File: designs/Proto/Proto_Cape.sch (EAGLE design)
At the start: 24 parts

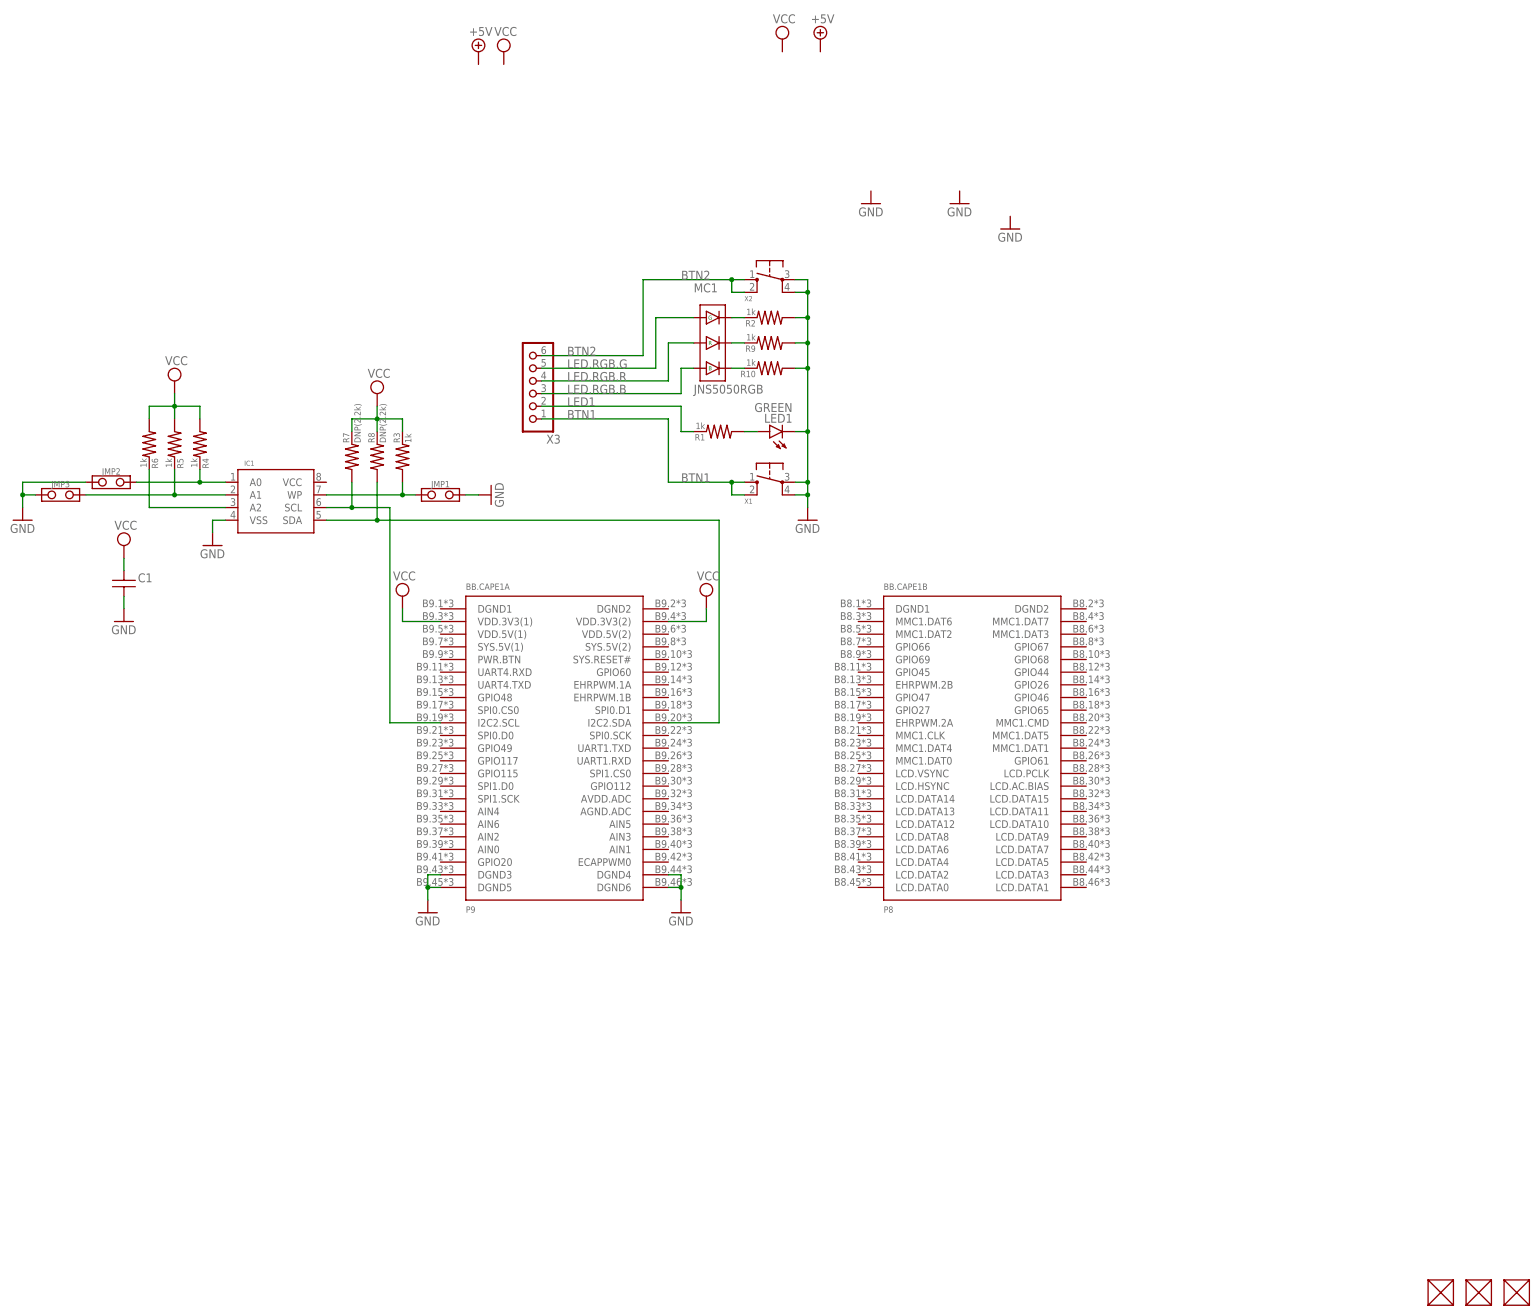
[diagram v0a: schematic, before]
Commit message: Added the revised EAGLE schematics. Also removed two files that were probably not intended to be added as they are lock files in EAGLE.
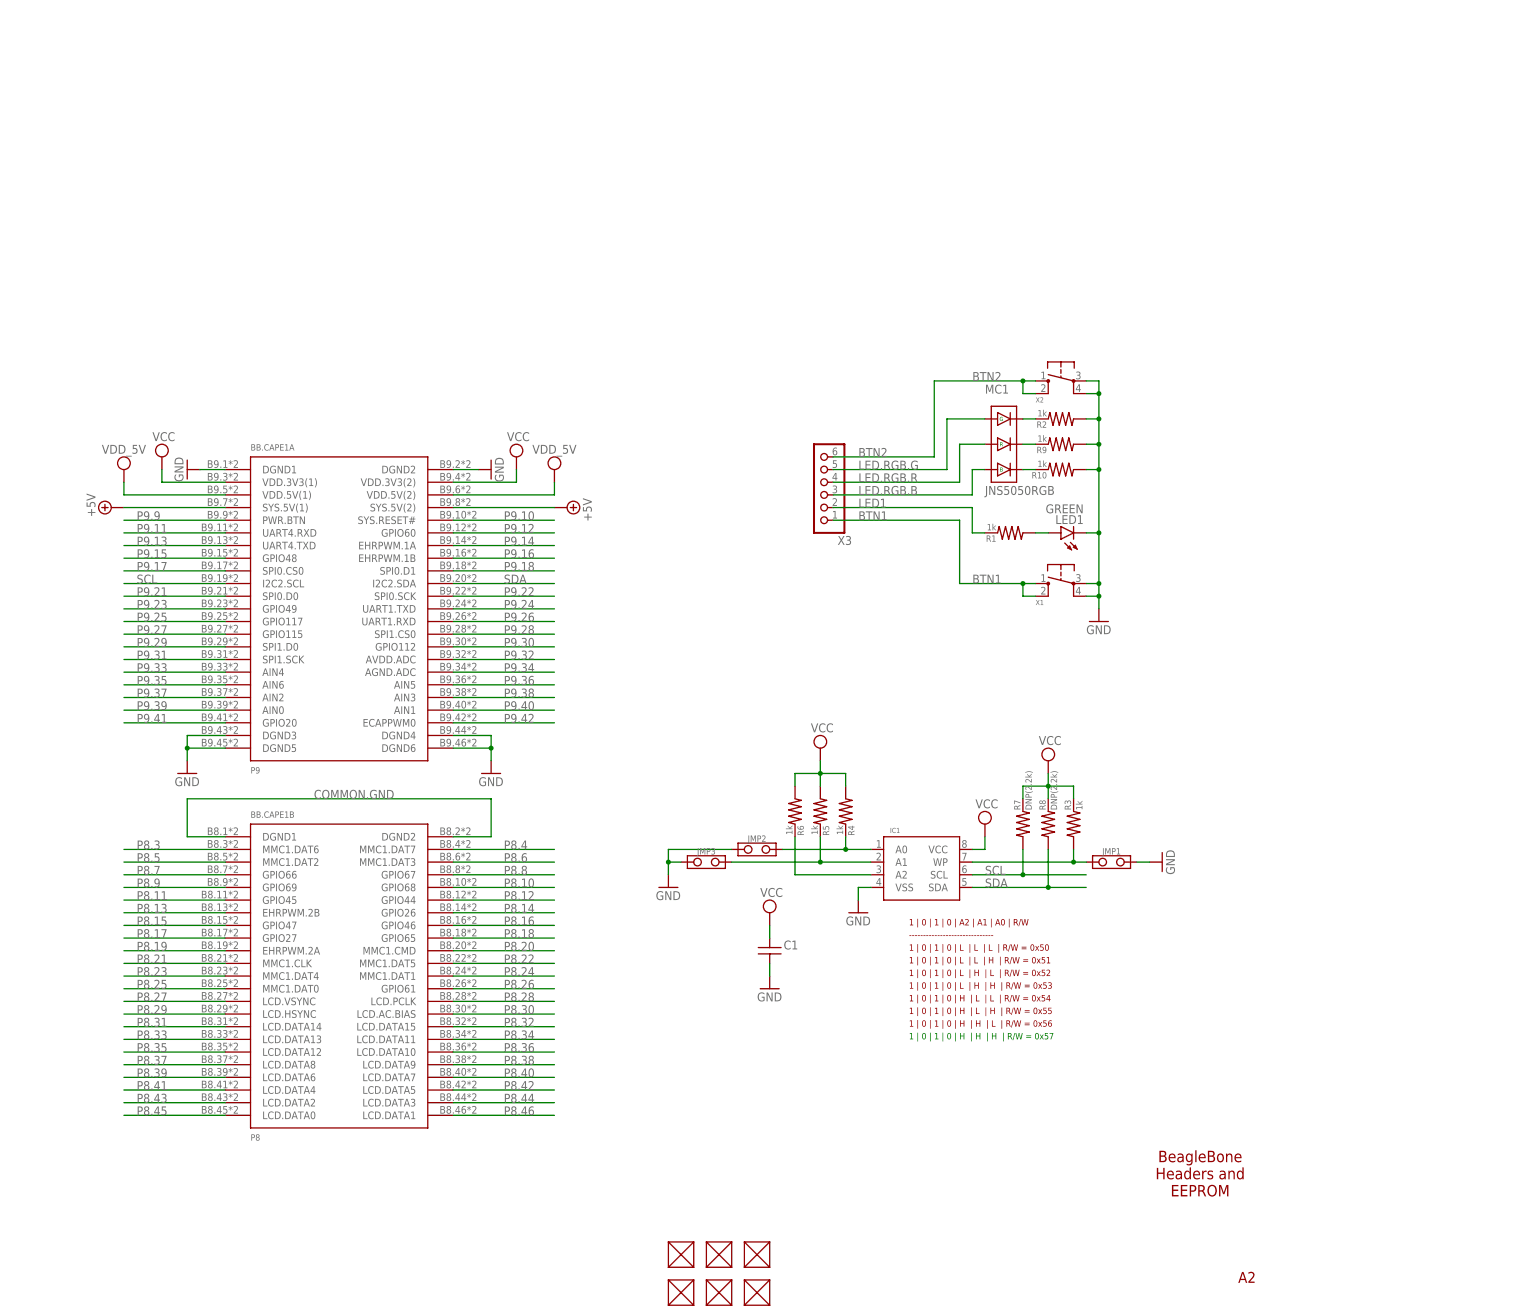
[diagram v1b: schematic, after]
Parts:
- added FUD4, FUD5, FUD6: FIDUCIAL, GHI:FIDUCIAL
- BB.CAPE1: value BEAGLEBONE.CAPE.TOP/BOTTOM-PADS/W/TH -> BEAGLEBONE.CAPE.TOP/BOTTOM-PADS; device GHI-Solutions:BEAGLEBONE.CAPE.TOP/BOTTOM-PADS/W/TH -> GHI-Solutions:BEAGLEBONE.CAPE.TOP/BOTTOM-PADS
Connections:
- new net +5V: BB.CAPE1A.SYS.5V(1), BB.CAPE1A.SYS.5V(2)
- new net COMMON.GND: BB.CAPE1B.DGND1, BB.CAPE1B.DGND2
- new net P8.10: BB.CAPE1B.GPIO68
- new net P8.11: BB.CAPE1B.GPIO45
- new net P8.12: BB.CAPE1B.GPIO44
- new net P8.13: BB.CAPE1B.EHRPWM.2B
- new net P8.14: BB.CAPE1B.GPIO26
- new net P8.15: BB.CAPE1B.GPIO47
- new net P8.16: BB.CAPE1B.GPIO46
- new net P8.17: BB.CAPE1B.GPIO27
- new net P8.18: BB.CAPE1B.GPIO65
- new net P8.19: BB.CAPE1B.EHRPWM.2A
- new net P8.20: BB.CAPE1B.MMC1.CMD
- new net P8.21: BB.CAPE1B.MMC1.CLK
- new net P8.22: BB.CAPE1B.MMC1.DAT5
- new net P8.23: BB.CAPE1B.MMC1.DAT4
- new net P8.24: BB.CAPE1B.MMC1.DAT1
- new net P8.25: BB.CAPE1B.MMC1.DAT0
- new net P8.26: BB.CAPE1B.GPIO61
- new net P8.27: BB.CAPE1B.LCD.VSYNC
- new net P8.28: BB.CAPE1B.LCD.PCLK
- new net P8.29: BB.CAPE1B.LCD.HSYNC
- new net P8.3: BB.CAPE1B.MMC1.DAT6
- new net P8.30: BB.CAPE1B.LCD.AC.BIAS
- new net P8.31: BB.CAPE1B.LCD.DATA14
- new net P8.32: BB.CAPE1B.LCD.DATA15
- new net P8.33: BB.CAPE1B.LCD.DATA13
- new net P8.34: BB.CAPE1B.LCD.DATA11
- new net P8.35: BB.CAPE1B.LCD.DATA12
- new net P8.36: BB.CAPE1B.LCD.DATA10
- new net P8.37: BB.CAPE1B.LCD.DATA8
- new net P8.38: BB.CAPE1B.LCD.DATA9
- new net P8.39: BB.CAPE1B.LCD.DATA6
- new net P8.4: BB.CAPE1B.MMC1.DAT7
- new net P8.40: BB.CAPE1B.LCD.DATA7
- new net P8.41: BB.CAPE1B.LCD.DATA4
- new net P8.42: BB.CAPE1B.LCD.DATA5
- new net P8.43: BB.CAPE1B.LCD.DATA2
- new net P8.44: BB.CAPE1B.LCD.DATA3
- new net P8.45: BB.CAPE1B.LCD.DATA0
- new net P8.46: BB.CAPE1B.LCD.DATA1
- new net P8.5: BB.CAPE1B.MMC1.DAT2
- new net P8.6: BB.CAPE1B.MMC1.DAT3
- new net P8.7: BB.CAPE1B.GPIO66
- new net P8.8: BB.CAPE1B.GPIO67
- new net P8.9: BB.CAPE1B.GPIO69
- new net P9.10: BB.CAPE1A.SYS.RESET#
- new net P9.11: BB.CAPE1A.UART4.RXD
- new net P9.12: BB.CAPE1A.GPIO60
- new net P9.13: BB.CAPE1A.UART4.TXD
- new net P9.14: BB.CAPE1A.EHRPWM.1A
- new net P9.15: BB.CAPE1A.GPIO48
- new net P9.16: BB.CAPE1A.EHRPWM.1B
- new net P9.17: BB.CAPE1A.SPI0.CS0
- new net P9.18: BB.CAPE1A.SPI0.D1
- new net P9.21: BB.CAPE1A.SPI0.D0
- new net P9.22: BB.CAPE1A.SPI0.SCK
- new net P9.23: BB.CAPE1A.GPIO49
- new net P9.24: BB.CAPE1A.UART1.TXD
- new net P9.25: BB.CAPE1A.GPIO117
- new net P9.26: BB.CAPE1A.UART1.RXD
- new net P9.27: BB.CAPE1A.GPIO115
- new net P9.28: BB.CAPE1A.SPI1.CS0
- new net P9.29: BB.CAPE1A.SPI1.D0
- new net P9.30: BB.CAPE1A.GPIO112
- new net P9.31: BB.CAPE1A.SPI1.SCK
- new net P9.32: BB.CAPE1A.AVDD.ADC
- new net P9.33: BB.CAPE1A.AIN4
- new net P9.34: BB.CAPE1A.AGND.ADC
- new net P9.35: BB.CAPE1A.AIN6
- new net P9.36: BB.CAPE1A.AIN5
- new net P9.37: BB.CAPE1A.AIN2
- new net P9.38: BB.CAPE1A.AIN3
- new net P9.39: BB.CAPE1A.AIN0
- new net P9.40: BB.CAPE1A.AIN1
- new net P9.41: BB.CAPE1A.GPIO20
- new net P9.42: BB.CAPE1A.ECAPPWM0
- new net P9.9: BB.CAPE1A.PWR.BTN
- new net VDD_5V: BB.CAPE1A.VDD.5V(1), BB.CAPE1A.VDD.5V(2)
- net GND: now also BB.CAPE1A.DGND1, BB.CAPE1A.DGND2
- net VCC: now also IC1.VCC
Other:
- note added: "------------------------------"
- note added: "1 | 0 | 1 | 0 | A2 | A1 | A0 | R/W"
- note added: "1 | 0 | 1 | 0 | H | H | H | R/W = 0x57"
- note added: "1 | 0 | 1 | 0 | H | H | L | R/W = 0x56"
- note added: "1 | 0 | 1 | 0 | H | L | H | R/W = 0x55"
- note added: "1 | 0 | 1 | 0 | H | L | L | R/W = 0x54"
- note added: "1 | 0 | 1 | 0 | L | H | H | R/W = 0x53"
- note added: "1 | 0 | 1 | 0 | L | H | L | R/W = 0x52"
- note added: "1 | 0 | 1 | 0 | L | L | H | R/W = 0x51"
- note added: "1 | 0 | 1 | 0 | L | L | L | R/W = 0x50"
- note added: "A2"
- note added: "BeagleBone Headers and EEPROM"
- moved on the sheet: BB.CAPE1A, BB.CAPE1B, C1, IC1, JMP1, JMP2, JMP3, LED1, MC1, R1, R10, R2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
